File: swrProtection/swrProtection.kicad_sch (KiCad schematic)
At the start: 18 parts, among them J1 Conn_01x02, J2 Conn_01x02, J3 Conn_01x02, J4 Conn_01x02, Q1 BSS123, U1 TLV4062/TLV4082, U2 74LVC2G00, U5 74LVC2G00

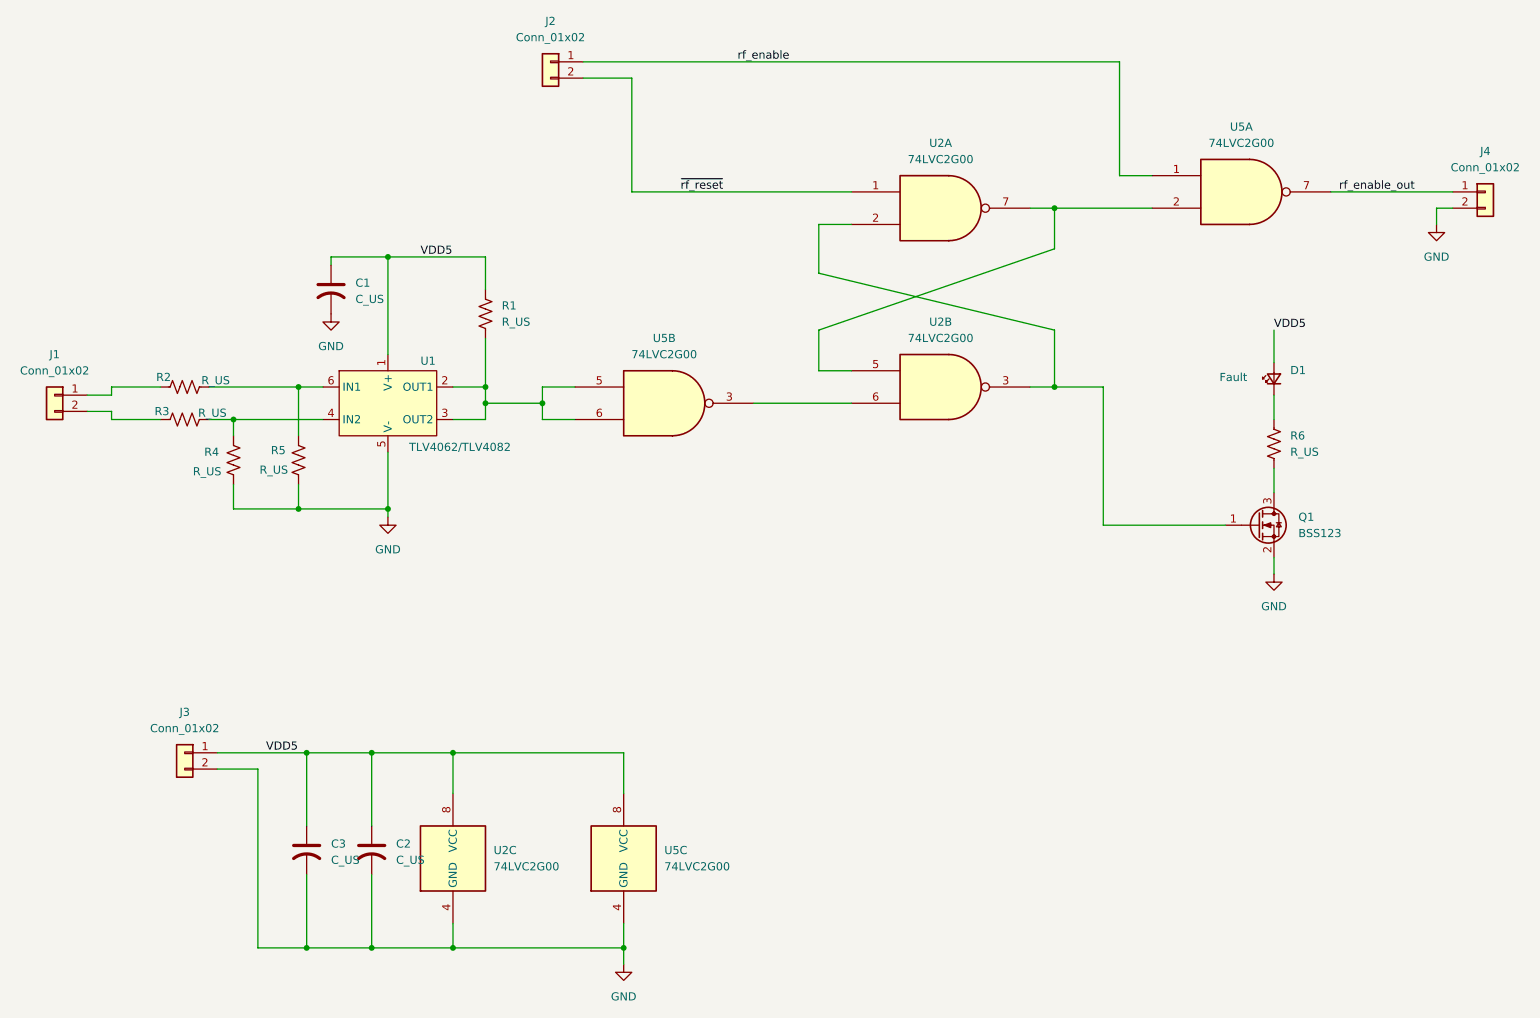
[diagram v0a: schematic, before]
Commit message: Tapeout of swr protection circuit
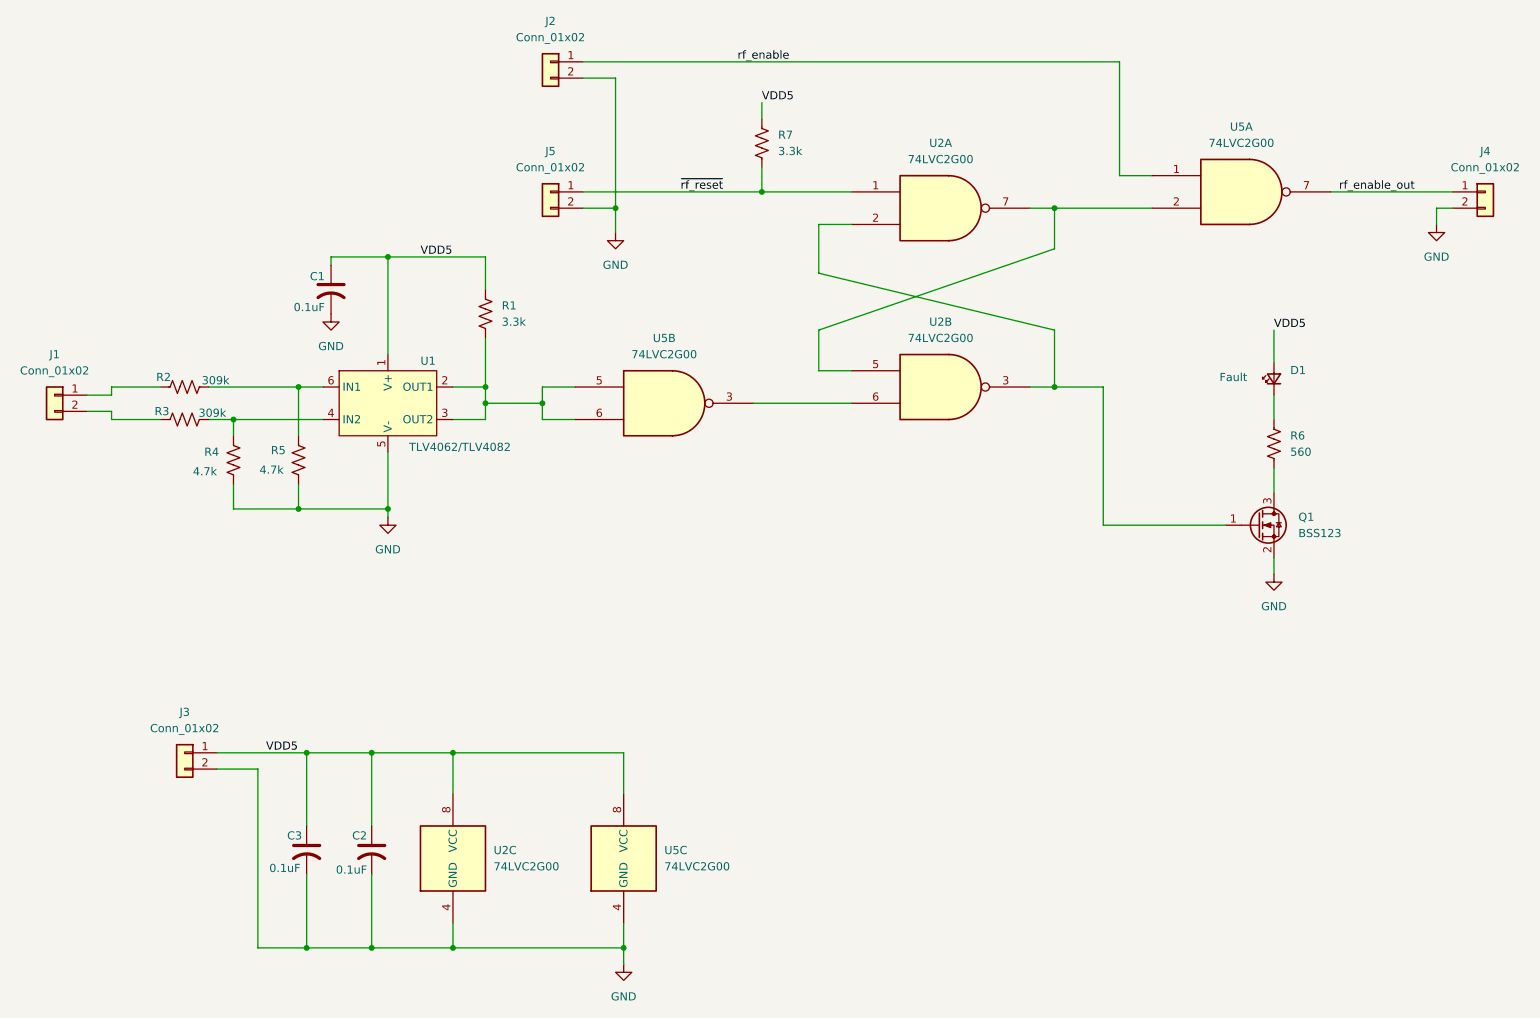
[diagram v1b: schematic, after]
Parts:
- added J5: Conn_01x02, Connector_PinHeader_2.54mm:PinHeader_1x02_P2.54mm_Vertical, symbol Connector_Generic:Conn_01x02
- added R7: 3.3k, Resistor_SMD:R_0603_1608Metric_Pad0.98x0.95mm_HandSolder, symbol Device:R_US
- C1, C2, C3: value C_US -> 0.1uF; footprint (none) -> Capacitor_SMD:C_0603_1608Metric_Pad1.08x0.95mm_HandSolder
- D1: footprint (none) -> LED_THT:LED_D5.0mm; MouserPN (none) -> 606-CMD333URC2
- J1, J2, J3, J4: footprint (none) -> Connector_PinHeader_2.54mm:PinHeader_1x02_P2.54mm_Vertical
- R1: value R_US -> 3.3k; footprint (none) -> Resistor_SMD:R_0603_1608Metric_Pad0.98x0.95mm_HandSolder
- R2, R3: value R_US -> 309k; footprint (none) -> Resistor_SMD:R_0603_1608Metric_Pad0.98x0.95mm_HandSolder
- R4, R5: value R_US -> 4.7k; footprint (none) -> Resistor_SMD:R_0603_1608Metric_Pad0.98x0.95mm_HandSolder
- R6: value R_US -> 560; footprint (none) -> Resistor_SMD:R_0603_1608Metric_Pad0.98x0.95mm_HandSolder
- U1: footprint (none) -> Package_TO_SOT_SMD:SOT-23-6_Handsoldering; MouserPN (none) -> 595-TLV4082DBVR
- U2: footprint (none) -> Package_SO:TSSOP-8_3x3mm_P0.65mm; MouserPN (none) -> 595-SN74LVC2G00DCTR
- U5: footprint (none) -> Package_SO:TSSOP-8_3x3mm_P0.65mm
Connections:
- net GND: now also J2.2 (Pin_2), J5.2 (Pin_2)
- net VDD5: now also R7.1
- net ~{rf_reset}: now also J5.1 (Pin_1), R7.2; no longer J2.2 (Pin_2)

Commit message: updated swr schematic and board
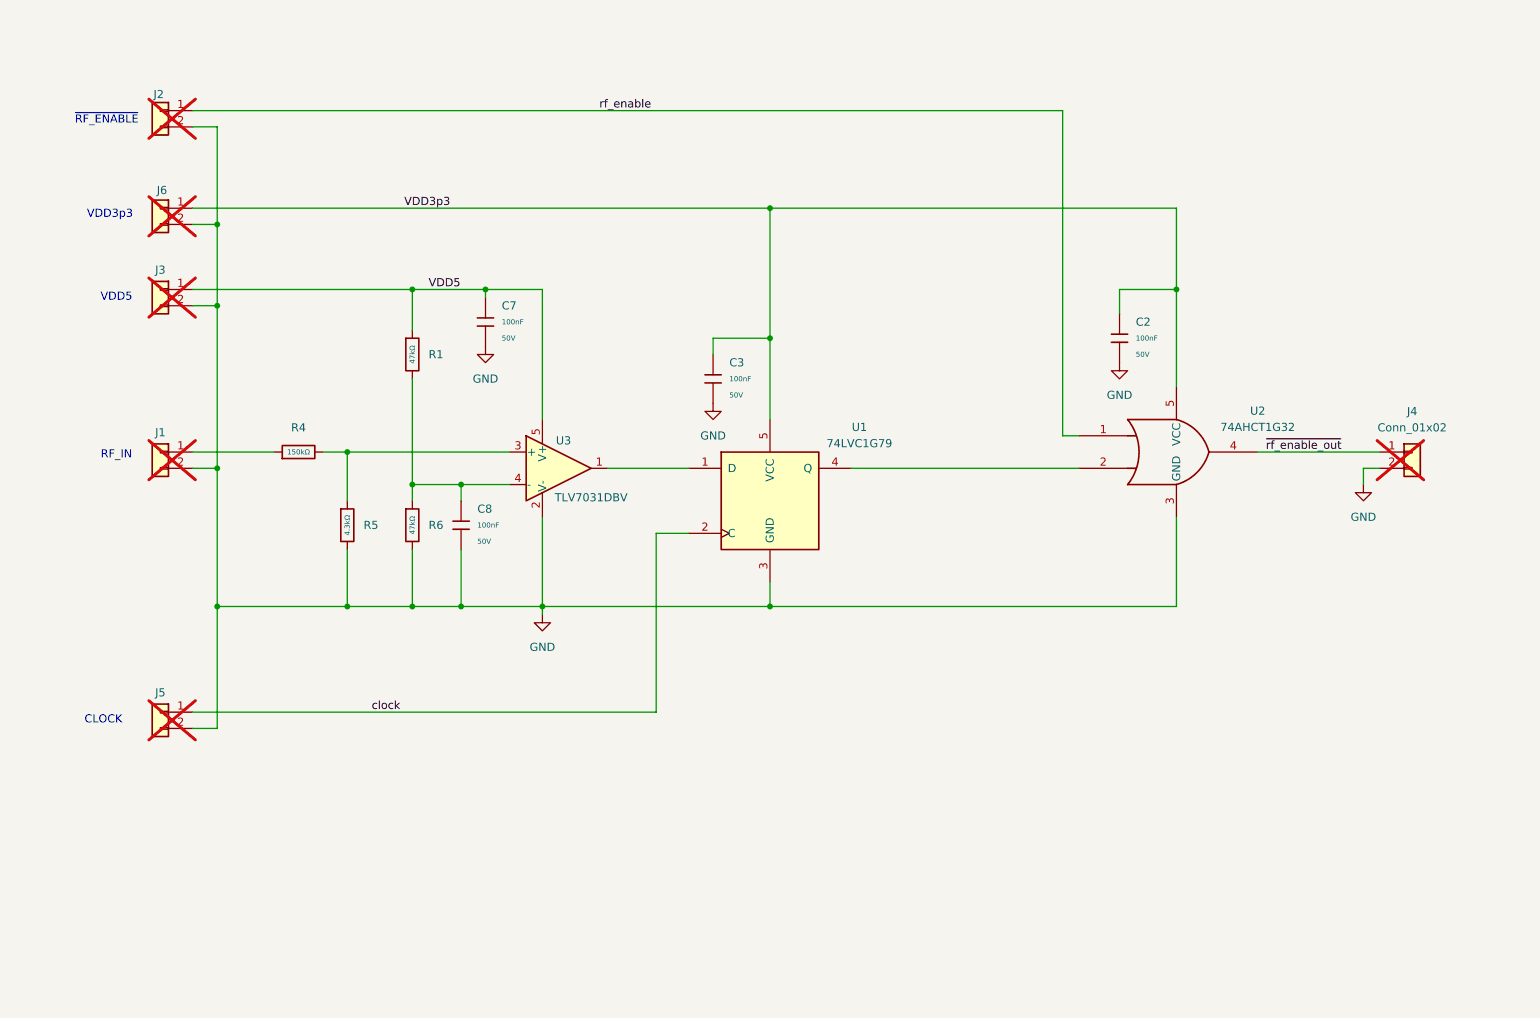
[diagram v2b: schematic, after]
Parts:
- removed C1, C2, C3: 0.1uF, Capacitor_SMD:C_0603_1608Metric_Pad1.08x0.95mm_HandSolder, symbol Device:C_US
- removed D1: LED_Small, LED_THT:LED_D5.0mm, symbol Device:LED_Small
- removed Q1: BSS123, Package_TO_SOT_SMD:SOT-23, symbol Transistor_FET:BSS123
- removed R1, R7: 3.3k, Resistor_SMD:R_0603_1608Metric_Pad0.98x0.95mm_HandSolder, symbol Device:R_US
- removed R2, R3: 309k, Resistor_SMD:R_0603_1608Metric_Pad0.98x0.95mm_HandSolder, symbol Device:R_US
- removed R4, R5: 4.7k, Resistor_SMD:R_0603_1608Metric_Pad0.98x0.95mm_HandSolder, symbol Device:R_US
- removed R6: 560, Resistor_SMD:R_0603_1608Metric_Pad0.98x0.95mm_HandSolder, symbol Device:R_US
- removed U1: TLV4062/TLV4082, Package_TO_SOT_SMD:SOT-23-6_Handsoldering, symbol EasyEDA:TLV4062
- removed U2, U5: 74LVC2G00, Package_SO:TSSOP-8_3x3mm_P0.65mm, symbol 74xGxx:74LVC2G00
- added C2, C3, C7, C8: 100nF, PCM_JLCPCB:C_0603, symbol PCM_JLCPCB-Capacitors:0603,100nF
- added J6: Conn_01x02, Connector_PinHeader_2.54mm:PinHeader_1x02_P2.54mm_Vertical, symbol Connector_Generic:Conn_01x02
- added R1, R6: 47kΩ, PCM_JLCPCB:R_0603, symbol PCM_JLCPCB-Resistors:0603,47kΩ
- added R4: 150kΩ, PCM_JLCPCB:R_0603, symbol PCM_JLCPCB-Resistors:0603,150kΩ
- added R5: 4.3kΩ, PCM_JLCPCB:R_0603, symbol PCM_JLCPCB-Resistors:0603,4.3kΩ
- added U1: 74LVC1G79, PCM_JLCPCB:SOT-23-5_L3.0-W1.7-P0.95-LS2.8-BR, symbol 74xGxx:74LVC1G79
- added U2: 74AHCT1G32, PCM_JLCPCB:SOT-23-5_L3.0-W1.7-P0.95-LS2.8-BR, symbol 74xGxx:74AHCT1G32
- added U3: TLV7031DBV, Package_TO_SOT_SMD:SOT-23-5, symbol Comparator:TLV7031DBV
- J1, J2, J3, J4, J5: now not fitted; now left out of the parts list
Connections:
- net GND: now also J1.2 (Pin_2), C2.2, C3.2, C7.2, C8.2, J6.2 (Pin_2), R5.2, R6.2, U1.3 (GND), U2.3 (GND), U3.2 (V-)
- net VDD5: now also C7.1, R1.1, U3.5 (V+)
- net rf_enable: now also U2.1
- net at J1.1 (Pin_1): now also R4.1
- net rf_enable_out renamed ~{rf_enable_out}
- net ~{rf_enable_out}: now also U2.4
- net ~{rf_reset} renamed clock
- net clock: now also U1.2 (C)
- new net: U1.1 (D), U3.1
- new net: R4.2, R5.1, U3.3 (+)
- new net: C8.1, R1.2, R6.1, U3.4 (-)
- new net: U1.4 (Q), U2.2
- new net VDD3p3: C2.1, C3.1, J6.1 (Pin_1), U1.5 (VCC), U2.5 (VCC)
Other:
- note added: "CLOCK"
- note added: "RF_IN"
- note added: "VDD3p3"
- note added: "VDD5"
- note added: "~{RF_ENABLE}"
- note removed: "Fault"

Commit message: swr protection final
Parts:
- removed U1: 74LVC1G79, PCM_JLCPCB:SOT-23-5_L3.0-W1.7-P0.95-LS2.8-BR, symbol 74xGxx:74LVC1G79
- removed U2: 74AHCT1G32, PCM_JLCPCB:SOT-23-5_L3.0-W1.7-P0.95-LS2.8-BR, symbol 74xGxx:74AHCT1G32
- added J7: Conn_01x01, Connector_PinHeader_2.54mm:PinHeader_1x01_P2.54mm_Vertical, symbol Connector_Generic:Conn_01x01
- added R2, R3: 47kΩ, PCM_JLCPCB:R_0603, symbol PCM_JLCPCB-Resistors:0603,47kΩ
- added U4: 74HCT74, Package_SO:SO-14_3.9x8.65mm_P1.27mm, symbol 74xx:74HCT74
- added U5: 74LVC1G32, Package_TO_SOT_SMD:SOT-23-5, symbol 74xGxx:74LVC1G32
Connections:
- net GND: now also U4.11 (C), U4.12 (D), U4.13 (~{R}), U4.7 (GND), U5.3 (GND)
- net VDD3p3: now also U5.5 (VCC); no longer C3.1
- net VDD5: now also C3.1, R2.1, R3.1, U4.14 (VCC)
- net ~{rf_enable_out}: now also U5.4
- net at U3.1: now also U4.3 (C)
- net clock renamed tx_enable
- net tx_enable: now also U4.1 (~{R})
- net rf_enable renamed ~{rf_enable}
- net ~{rf_enable}: now also U5.1
- new net: J7.1 (Pin_1), U4.6 (~{Q})
- new net: U4.5 (Q), U5.2
- new net: R2.2, U4.2 (D), U4.4 (~{S})
- new net: R3.2, U4.10 (~{S})
- no-connect marks 0 -> 2
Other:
- note added: "TX_ENABLE"
- note removed: "CLOCK"
- moved on the sheet: C2, C3, J4
